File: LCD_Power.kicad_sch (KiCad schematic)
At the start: 22 parts, among them Q2 Q_PMOS_GSD, Q3 Q_PMOS_GSD, U6 SY7200AABC

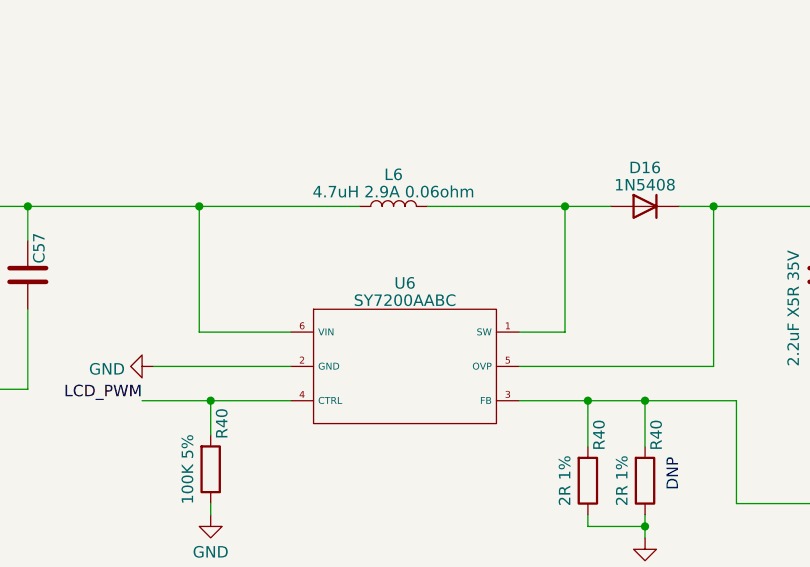
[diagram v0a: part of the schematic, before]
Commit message: updated footprints
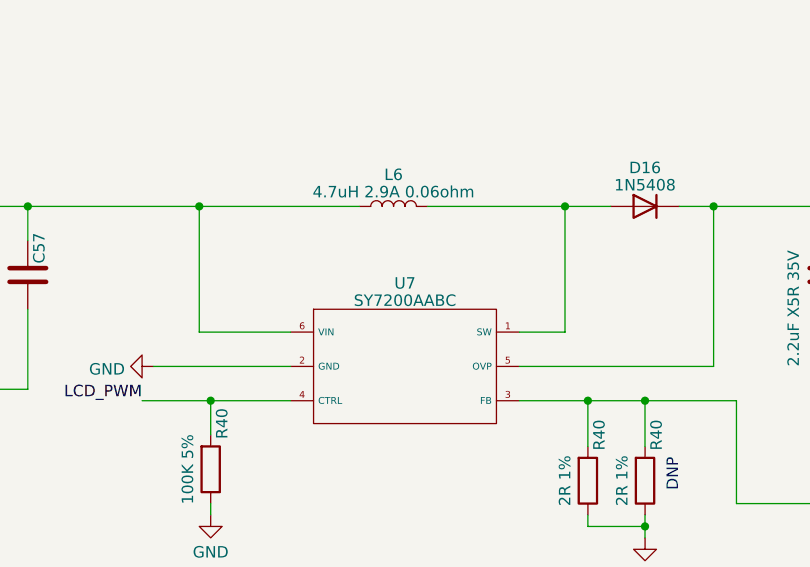
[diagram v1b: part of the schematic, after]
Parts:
- renumbered U6 to U7

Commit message: updated Reference, and PCB
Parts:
- removed D16: 1N5408, Diode_THT:D_DO-201AD_P15.24mm_Horizontal, symbol Diode:1N5408
- added D16: 1N5400, Diode_SMD:D_SOD-323, symbol Diode:1N5400
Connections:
- net VCC_LED+: now also D16.1 (K)
- net at L6.2, U7.1 (SW): now also D16.2 (A)
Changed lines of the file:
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@@
-    )
-  )
-  (symbol (lib_id "Diode:1N5408") (at 190.5 116.84 0) (mirror y) (unit 1)
-    (in_bom yes) (on_board yes) (dnp no) (fields_autoplaced)
-    (property "Reference" "D16" (at 190.5 112.5601 0)
-      (effects (font (size 1.27 1.27)))
-    )
-    (property "Value" "1N5408" (at 190.5 114.4811 0)
-      (effects (font (size 1.27 1.27)))
-    )
-    (property "Footprint" "Diode_THT:D_DO-201AD_P15.24mm_Horizontal" (at 190.5 121.285 0)
-      (effects (font (size 1.27 1.27)) hide)
-    )
-    (property "Datasheet" "http://www.vishay.com/docs/88516/1n5400.pdf" (at 190.5 116.84 0)
-      (effects (font (size 1.27 1.27)) hide)
-    )
-    (property "Sim.Device" "D" (at 190.5 116.84 0)
-      (effects (font (size 1.27 1.27)) hide)
-    )
-    (property "Sim.Pins" "1=K 2=A" (at 190.5 116.84 0)
-      (effects (font (size 1.27 1.27)) hide)
-    )
-    (pin "1")
-    (pin "2")
-    (instances
-      (project "leaf"
-        (path "/e3b58043-16a3-43c8-9fad-9c9784eebfa4/abba4c44-e9bc-404f-bbc8-3409461eb15e/42834052-256a-43ae-b5b1-2328aa6298dd"
-          (reference "D16") (unit 1)
-        )
-      )
     )
   )
@@
         )
       )
+    )
+  )
+  (symbol (lib_id "Diode:1N5400") (at 190.5 116.84 0) (mirror y) (unit 1)
+    (in_bom yes) (on_board yes) (dnp no) (fields_autoplaced)
+    (property "Reference" "D16" (at 190.5 112.5601 0)
+      (effects (font (size 1.27 1.27)))
+    )
+    (property "Value" "1N5400" (at 190.5 114.4811 0)
+      (effects (font (size 1.27 1.27)))
+    )
+    (property "Footprint" "Diode_SMD:D_SOD-323" (at 190.5 121.285 0)
+      (effects (font (size 1.27 1.27)) hide)
+    )
+    (property "Datasheet" "http://www.vishay.com/docs/88516/1n5400.pdf" (at 190.5 116.84 0)
+      (effects (font (size 1.27 1.27)) hide)
+    )
+    (property "Sim.Device" "D" (at 190.5 116.84 0)
+      (effects (font (size 1.27 1.27)) hide)
+    )
+    (property "Sim.Pins" "1=K 2=A" (at 190.5 116.84 0)
+      (effects (font (size 1.27 1.27)) hide)
+    )
+    (pin "1")
+    (pin "2")
+    (instances
+      (project "leaf"
+        (path "/e3b58043-16a3-43c8-9fad-9c9784eebfa4/abba4c44-e9bc-404f-bbc8-3409461eb15e/42834052-256a-43ae-b5b1-2328aa6298dd"
+          (reference "D16") (unit 1)
+        )
+      )

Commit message: updated Capacitors
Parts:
- C57: LCSC (none) -> C77004; Model (none) -> GRM155R61A475KEAAD; Vendor (none) -> muRata(村田)
- C57: footprint Capacitor_SMD:C_0402_1005Metric -> Capacitor_SMD:C_0201_0603Metric; LCSC (none) -> C76934; Model (none) -> GRM033R61A104KE15D; Vendor (none) -> muRata(村田)
- C57: value 4.7uF X5R 6.3V -> 4.7uF X5R 10V; LCSC (none) -> C77004; Model (none) -> GRM155R61A475KEAAD; Vendor (none) -> muRata(村田)
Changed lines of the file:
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@@
+      (effects (font (size 1.27 1.27)) hide)
+    )
+    (property "Description" "容值: 4.7uF 精度: ±10% 额定电压: 10V 材质(温度系数): X5R 材质:X5R" (at 110.49 124.46 0)
+      (effects (font (size 1.27 1.27)) hide)
+    )
+    (property "LCSC" "C77004" (at 110.49 124.46 0)
+      (effects (font (size 1.27 1.27)) hide)
+    )
+    (property "Model" "GRM155R61A475KEAAD" (at 110.49 124.46 0)
+      (effects (font (size 1.27 1.27)) hide)
+    )
+    (property "Vendor" "muRata(村田) " (at 110.49 124.46 0)
       (effects (font (size 1.27 1.27)) hide)
     )
@@
       (effects (font (size 1.27 1.27)) (justify left))
     )
-    (property "Footprint" "Capacitor_SMD:C_0402_1005Metric" (at 215.5952 55.88 0)
+    (property "Footprint" "Capacitor_SMD:C_0201_0603Metric" (at 215.5952 55.88 0)
       (effects (font (size 1.27 1.27)) hide)
     )
     (property "Datasheet" "~" (at 214.63 52.07 0)
+      (effects (font (size 1.27 1.27)) hide)
+    )
+    (property "Description" "容值: 100nF 精度: ±10% 额定电压: 10V 材质(温度系数): X5R 材质:X5R" (at 214.63 52.07 0)
+      (effects (font (size 1.27 1.27)) hide)
+    )
+    (property "LCSC" "C76934" (at 214.63 52.07 0)
+      (effects (font (size 1.27 1.27)) hide)
+    )
+    (property "Model" "GRM033R61A104KE15D" (at 214.63 52.07 0)
+      (effects (font (size 1.27 1.27)) hide)
+    )
+    (property "Vendor" "muRata(村田)" (at 214.63 52.07 0)
       (effects (font (size 1.27 1.27)) hide)
     )
@@
       (effects (font (size 1.27 1.27)) (justify left))
     )
-    (property "Value" "4.7uF X5R 6.3V" (at 138.43 62.23 90)
+    (property "Value" "4.7uF X5R 10V" (at 138.43 62.23 90)
       (effects (font (size 1.27 1.27)) (justify left))
     )
@@
     )
     (property "Datasheet" "~" (at 142.24 52.07 0)
+      (effects (font (size 1.27 1.27)) hide)
+    )
+    (property "Description" "容值: 4.7uF 精度: ±10% 额定电压: 10V 材质(温度系数): X5R 材质:X5R" (at 142.24 52.07 0)
+      (effects (font (size 1.27 1.27)) hide)
+    )
+    (property "LCSC" "C77004" (at 142.24 52.07 0)
+      (effects (font (size 1.27 1.27)) hide)
+    )
+    (property "Model" "GRM155R61A475KEAAD" (at 142.24 52.07 0)
+      (effects (font (size 1.27 1.27)) hide)
+    )
+    (property "Vendor" "muRata(村田) " (at 142.24 52.07 0)
       (effects (font (size 1.27 1.27)) hide)
     )
@@
       (effects (font (size 1.27 1.27)) (justify left))
     )
-    (property "Footprint" "Capacitor_SMD:C_0402_1005Metric" (at 122.8852 128.27 0)
+    (property "Footprint" "Capacitor_SMD:C_0201_0603Metric" (at 122.8852 128.27 0)
       (effects (font (size 1.27 1.27)) hide)
     )
     (property "Datasheet" "~" (at 121.92 124.46 0)
+      (effects (font (size 1.27 1.27)) hide)
+    )
+    (property "Description" "容值: 100nF 精度: ±10% 额定电压: 10V 材质(温度系数): X5R 材质:X5R" (at 121.92 124.46 0)
+      (effects (font (size 1.27 1.27)) hide)
+    )
+    (property "LCSC" "C76934" (at 121.92 124.46 0)
+      (effects (font (size 1.27 1.27)) hide)
+    )
+    (property "Model" "GRM033R61A104KE15D" (at 121.92 124.46 0)
+      (effects (font (size 1.27 1.27)) hide)
+    )
+    (property "Vendor" "muRata(村田)" (at 121.92 124.46 0)
       (effects (font (size 1.27 1.27)) hide)
     )
@@
       (effects (font (size 1.27 1.27)) (justify left))
     )
-    (property "Footprint" "Capacitor_SMD:C_0402_1005Metric" (at 117.8052 54.61 0)
+    (property "Footprint" "Capacitor_SMD:C_0201_0603Metric" (at 117.8052 54.61 0)
       (effects (font (size 1.27 1.27)) hide)
     )
     (property "Datasheet" "~" (at 116.84 50.8 0)
+      (effects (font (size 1.27 1.27)) hide)
+    )
+    (property "Description" "容值: 100nF 精度: ±10% 额定电压: 10V 材质(温度系数): X5R 材质:X5R" (at 116.84 50.8 0)
+      (effects (font (size 1.27 1.27)) hide)
+    )
+    (property "LCSC" "C76934" (at 116.84 50.8 0)
+      (effects (font (size 1.27 1.27)) hide)
+    )
+    (property "Model" "GRM033R61A104KE15D" (at 116.84 50.8 0)
+      (effects (font (size 1.27 1.27)) hide)
+    )
+    (property "Vendor" "muRata(村田)" (at 116.84 50.8 0)
       (effects (font (size 1.27 1.27)) hide)
     )
@@
       (effects (font (size 1.27 1.27)) (justify left))
     )
-    (property "Value" "4.7uF X5R 6.3V" (at 236.22 63.5 90)
+    (property "Value" "4.7uF X5R 10V" (at 236.22 63.5 90)
       (effects (font (size 1.27 1.27)) (justify left))
     )
@@
       (effects (font (size 1.27 1.27)) hide)
     )
+    (property "Description" "容值: 4.7uF 精度: ±10% 额定电压: 10V 材质(温度系数): X5R 材质:X5R" (at 240.03 53.34 0)
+      (effects (font (size 1.27 1.27)) hide)
+    )
+    (property "LCSC" "C77004" (at 240.03 53.34 0)
+      (effects (font (size 1.27 1.27)) hide)
+    )
+    (property "Model" "GRM155R61A475KEAAD" (at 240.03 53.34 0)
+      (effects (font (size 1.27 1.27)) hide)
+    )
+    (property "Vendor" "muRata(村田) " (at 240.03 53.34 0)
+      (effects (font (size 1.27 1.27)) hide)
+    )

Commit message: updated LCSC selection of capacitors
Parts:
- C57: LCSC (none) -> C237392; Model (none) -> GRM155R6YA225KE11D; Vendor (none) -> muRata(村田)
- C57: LCSC (none) -> C77020; Model (none) -> GRM155R71H104KE14D; Vendor (none) -> muRata(村田)
- Q2, Q3: footprint (none) -> Package_TO_SOT_SMD:SOT-23-3
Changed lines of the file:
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@@
       (effects (font (size 1.27 1.27)))
     )
-    (property "Footprint" "" (at 130.81 34.29 0)
+    (property "Footprint" "Package_TO_SOT_SMD:SOT-23-3" (at 130.81 34.29 0)
       (effects (font (size 1.27 1.27)) hide)
     )
@@
       (effects (font (size 1.27 1.27)) hide)
     )
+    (property "Description" "容值: 2.2uF 精度: ±10% 额定电压: 35V 材质(温度系数): X5R 材质:X5R" (at 210.82 124.46 0)
+      (effects (font (size 1.27 1.27)) hide)
+    )
+    (property "LCSC" "C237392" (at 210.82 124.46 0)
+      (effects (font (size 1.27 1.27)) hide)
+    )
+    (property "Model" "GRM155R6YA225KE11D" (at 210.82 124.46 0)
+      (effects (font (size 1.27 1.27)) hide)
+    )
+    (property "Vendor" "muRata(村田)" (at 210.82 124.46 0)
+      (effects (font (size 1.27 1.27)) hide)
+    )
     (pin "1")
     (pin "2")
@@
     )
     (property "Datasheet" "~" (at 248.92 53.34 0)
+      (effects (font (size 1.27 1.27)) hide)
+    )
+    (property "Description" "容值: 100nF 精度: ±10% 额定电压: 50V 材质(温度系数): X7R 材质:X7R" (at 248.92 53.34 0)
+      (effects (font (size 1.27 1.27)) hide)
+    )
+    (property "LCSC" "C77020" (at 248.92 53.34 0)
+      (effects (font (size 1.27 1.27)) hide)
+    )
+    (property "Model" "GRM155R71H104KE14D" (at 248.92 53.34 0)
+      (effects (font (size 1.27 1.27)) hide)
+    )
+    (property "Vendor" "muRata(村田)" (at 248.92 53.34 0)
       (effects (font (size 1.27 1.27)) hide)
     )
@@
       (effects (font (size 1.27 1.27)) hide)
     )
+    (property "Description" "容值: 100nF 精度: ±10% 额定电压: 50V 材质(温度系数): X7R 材质:X7R" (at 224.79 124.46 0)
+      (effects (font (size 1.27 1.27)) hide)
+    )
+    (property "LCSC" "C77020" (at 224.79 124.46 0)
+      (effects (font (size 1.27 1.27)) hide)
+    )
+    (property "Model" "GRM155R71H104KE14D" (at 224.79 124.46 0)
+      (effects (font (size 1.27 1.27)) hide)
+    )
+    (property "Vendor" "muRata(村田)" (at 224.79 124.46 0)
+      (effects (font (size 1.27 1.27)) hide)
+    )
     (pin "1")
     (pin "2")
@@
       (effects (font (size 1.27 1.27)) hide)
     )
+    (property "Description" "容值: 100nF 精度: ±10% 额定电压: 50V 材质(温度系数): X7R 材质:X7R" (at 151.13 52.07 0)
+      (effects (font (size 1.27 1.27)) hide)
+    )
+    (property "LCSC" "C77020" (at 151.13 52.07 0)
+      (effects (font (size 1.27 1.27)) hide)
+    )
+    (property "Model" "GRM155R71H104KE14D" (at 151.13 52.07 0)
+      (effects (font (size 1.27 1.27)) hide)
+    )
+    (property "Vendor" "muRata(村田)" (at 151.13 52.07 0)
+      (effects (font (size 1.27 1.27)) hide)
+    )
     (pin "1")
     (pin "2")
@@
       (effects (font (size 1.27 1.27)))
     )
-    (property "Footprint" "" (at 228.6 35.56 0)
-      (effects (font (size 1.27 1.27)) hide)
-    )
+    (property "Footprint" "Package_TO_SOT_SMD:SOT-23-3" (at 228.6 35.56 0)
+      (effects (font (size 1.27 1.27)) hide)
+    )

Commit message: updated foorprints
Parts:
- D16: value 1N5400 -> SS34 40V 3A; footprint Diode_SMD:D_SOD-323 -> Diode_SMD:D_SMA; LCSC (none) -> C8678; Model (none) -> SS34; Vendor (none) -> MDD
- L6: LCSC (none) -> C3002636; Model (none) -> CKST0603-4.7uH/M; Vendor (none) -> CENKER(岑科)
- U7: footprint (none) -> Package_TO_SOT_SMD:SOT-23-6; LCSC (none) -> C107309; Model (none) -> SY7200AABC
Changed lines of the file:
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@@
       (effects (font (size 1.27 1.27)))
     )
-    (property "Footprint" "" (at 163.83 134.62 0)
+    (property "Footprint" "Package_TO_SOT_SMD:SOT-23-6" (at 163.83 134.62 0)
       (effects (font (size 1.27 1.27)) hide)
     )
     (property "Datasheet" "" (at 163.83 134.62 0)
+      (effects (font (size 1.27 1.27)) hide)
+    )
+    (property "LCSC" "C107309" (at 163.83 134.62 0)
+      (effects (font (size 1.27 1.27)) hide)
+    )
+    (property "Model" "SY7200AABC" (at 163.83 134.62 0)
       (effects (font (size 1.27 1.27)) hide)
     )
@@
       (effects (font (size 1.27 1.27)) hide)
     )
+    (property "Description" "电感值: 4.7uH 精度: ±20% 额定电流: 5A 饱和电流(Isat): 6.5A 直流电阻(DCR): 38mΩ" (at 162.56 116.84 0)
+      (effects (font (size 1.27 1.27)) hide)
+    )
+    (property "LCSC" "C3002636" (at 162.56 116.84 0)
+      (effects (font (size 1.27 1.27)) hide)
+    )
+    (property "Model" "CKST0603-4.7uH/M" (at 162.56 116.84 0)
+      (effects (font (size 1.27 1.27)) hide)
+    )
+    (property "Vendor" "CENKER(岑科)" (at 162.56 116.84 0)
+      (effects (font (size 1.27 1.27)) hide)
+    )
     (pin "1")
     (pin "2")
@@
       (effects (font (size 1.27 1.27)))
     )
-    (property "Value" "1N5400" (at 190.5 114.4811 0)
-      (effects (font (size 1.27 1.27)))
-    )
-    (property "Footprint" "Diode_SMD:D_SOD-323" (at 190.5 121.285 0)
-      (effects (font (size 1.27 1.27)) hide)
-    )
-    (property "Datasheet" "http://www.vishay.com/docs/88516/1n5400.pdf" (at 190.5 116.84 0)
-      (effects (font (size 1.27 1.27)) hide)
-    )
-    (property "Sim.Device" "D" (at 190.5 116.84 0)
-      (effects (font (size 1.27 1.27)) hide)
-    )
-    (property "Sim.Pins" "1=K 2=A" (at 190.5 116.84 0)
-      (effects (font (size 1.27 1.27)) hide)
-    )
+    (property "Value" "SS34 40V 3A" (at 190.5 114.4811 0)
+      (effects (font (size 1.27 1.27)))
+    )
+    (property "Footprint" "Diode_SMD:D_SMA" (at 190.5 121.285 0)
+      (effects (font (size 1.27 1.27)) hide)
+    )
+    (property "Datasheet" "" (at 190.5 116.84 0)
+      (effects (font (size 1.27 1.27)) hide)
+    )
+    (property "Sim.Device" "" (at 190.5 116.84 0)
+      (effects (font (size 1.27 1.27)) hide)
+    )
+    (property "Sim.Pins" "" (at 190.5 116.84 0)
+      (effects (font (size 1.27 1.27)) hide)
+    )
+    (property "Description" "二极管配置: 独立式 直流反向耐压(Vr): 40V 平均整流电流(Io): 3A 正向压降(Vf): 0.55V@3A 反向电流(Ir):" (at 190.5 116.84 0)
+      (effects (font (size 1.27 1.27)) hide)
+    )
+    (property "LCSC" "C8678" (at 190.5 116.84 0)
+      (effects (font (size 1.27 1.27)) hide)
+    )
+    (property "Model" "SS34" (at 190.5 116.84 0)
+      (effects (font (size 1.27 1.27)) hide)
+    )
+    (property "Vendor" "MDD" (at 190.5 116.84 0)
+      (effects (font (size 1.27 1.27)) hide)
+    )

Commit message: layout SoC Power and DDR capacitors
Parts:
- C57: LCSC C76934 -> C76928; Model GRM033R61A104KE15D -> GRM033R60J104KE19D
- C57: value 100nF X5R 10V -> 100nF X5R 6.3V; LCSC C76934 -> C76928; Model GRM033R61A104KE15D -> GRM033R60J104KE19D
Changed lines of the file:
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@@
       (effects (font (size 1.27 1.27)) hide)
     )
-    (property "Description" "容值: 100nF 精度: ±10% 额定电压: 10V 材质(温度系数): X5R 材质:X5R" (at 214.63 52.07 0)
-      (effects (font (size 1.27 1.27)) hide)
-    )
-    (property "LCSC" "C76934" (at 214.63 52.07 0)
-      (effects (font (size 1.27 1.27)) hide)
-    )
-    (property "Model" "GRM033R61A104KE15D" (at 214.63 52.07 0)
+    (property "Description" "容值: 100nF 精度: ±10% 额定电压: 6.3V 材质(温度系数): X5R 材质:X5R" (at 214.63 52.07 0)
+      (effects (font (size 1.27 1.27)) hide)
+    )
+    (property "LCSC" "C76928" (at 214.63 52.07 0)
+      (effects (font (size 1.27 1.27)) hide)
+    )
+    (property "Model" "GRM033R60J104KE19D" (at 214.63 52.07 0)
       (effects (font (size 1.27 1.27)) hide)
     )
@@
       (effects (font (size 1.27 1.27)) (justify left))
     )
-    (property "Value" "100nF X5R 10V" (at 118.11 134.62 90)
+    (property "Value" "100nF X5R 6.3V" (at 118.11 134.62 90)
       (effects (font (size 1.27 1.27)) (justify left))
     )
@@
       (effects (font (size 1.27 1.27)) hide)
     )
-    (property "Description" "容值: 100nF 精度: ±10% 额定电压: 10V 材质(温度系数): X5R 材质:X5R" (at 121.92 124.46 0)
-      (effects (font (size 1.27 1.27)) hide)
-    )
-    (property "LCSC" "C76934" (at 121.92 124.46 0)
-      (effects (font (size 1.27 1.27)) hide)
-    )
-    (property "Model" "GRM033R61A104KE15D" (at 121.92 124.46 0)
+    (property "Description" "容值: 100nF 精度: ±10% 额定电压: 6.3V 材质(温度系数): X5R 材质:X5R" (at 121.92 124.46 0)
+      (effects (font (size 1.27 1.27)) hide)
+    )
+    (property "LCSC" "C76928" (at 121.92 124.46 0)
+      (effects (font (size 1.27 1.27)) hide)
+    )
+    (property "Model" "GRM033R60J104KE19D" (at 121.92 124.46 0)
       (effects (font (size 1.27 1.27)) hide)
     )
@@
       (effects (font (size 1.27 1.27)) hide)
     )
-    (property "Description" "容值: 100nF 精度: ±10% 额定电压: 10V 材质(温度系数): X5R 材质:X5R" (at 116.84 50.8 0)
-      (effects (font (size 1.27 1.27)) hide)
-    )
-    (property "LCSC" "C76934" (at 116.84 50.8 0)
-      (effects (font (size 1.27 1.27)) hide)
-    )
-    (property "Model" "GRM033R61A104KE15D" (at 116.84 50.8 0)
-      (effects (font (size 1.27 1.27)) hide)
-    )
+    (property "Description" "容值: 100nF 精度: ±10% 额定电压: 6.3V 材质(温度系数): X5R 材质:X5R" (at 116.84 50.8 0)
+      (effects (font (size 1.27 1.27)) hide)
+    )
+    (property "LCSC" "C76928" (at 116.84 50.8 0)
+      (effects (font (size 1.27 1.27)) hide)
+    )
+    (property "Model" "GRM033R60J104KE19D" (at 116.84 50.8 0)
+      (effects (font (size 1.27 1.27)) hide)
+    )

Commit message: fix some ERCs
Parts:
- renumbered C57 to C?, Q3 to Q?, Q2 to Q?, R40 to R?

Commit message: fix ERC
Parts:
- R?: now not fitted
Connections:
- net VCC_1V8: now also C?.1
- net VCC_3V3: now also C?.1
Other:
- note removed: "DNP"
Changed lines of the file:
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@@
   (junction (at 110.49 116.84) (diameter 0) (color 0 0 0 0)
   )
+  (junction (at 116.84 36.83) (diameter 0) (color 0 0 0 0)
+  )
   (junction (at 198.12 116.84) (diameter 0) (color 0 0 0 0)
   )
@@
   (junction (at 240.03 64.77) (diameter 0) (color 0 0 0 0)
   )
+  (junction (at 214.63 38.1) (diameter 0) (color 0 0 0 0)
+  )
   (junction (at 203.2 62.23) (diameter 0) (color 0 0 0 0)
   )
@@
     (stroke (width 0) (type default))
   )
-  (wire (pts (xy 203.2 38.1) (xy 220.98 38.1))
+  (wire (pts (xy 203.2 38.1) (xy 214.63 38.1))
     (stroke (width 0) (type default))
   )
@@
     (stroke (width 0) (type default))
   )
-  (wire (pts (xy 105.41 36.83) (xy 123.19 36.83))
+  (wire (pts (xy 105.41 36.83) (xy 116.84 36.83))
     (stroke (width 0) (type default))
   )
@@
     (stroke (width 0) (type default))
   )
+  (wire (pts (xy 116.84 36.83) (xy 123.19 36.83))
+    (stroke (width 0) (type default))
+  )
   (wire (pts (xy 142.24 149.86) (xy 142.24 151.13))
     (stroke (width 0) (type default))
@@
     (stroke (width 0) (type default))
   )
+  (wire (pts (xy 214.63 48.26) (xy 214.63 38.1))
+    (stroke (width 0) (type default))
+  )
   (wire (pts (xy 116.84 60.96) (xy 128.27 60.96))
     (stroke (width 0) (type default))
@@
     (stroke (width 0) (type default))
   )
+  (wire (pts (xy 116.84 36.83) (xy 116.84 46.99))
+    (stroke (width 0) (type default))
+  )
   (wire (pts (xy 134.62 138.43) (xy 142.24 138.43))
     (stroke (width 0) (type default))
@@
   )
   (wire (pts (xy 224.79 135.89) (xy 210.82 135.89))
+    (stroke (width 0) (type default))
+  )
+  (wire (pts (xy 214.63 38.1) (xy 220.98 38.1))
     (stroke (width 0) (type default))
   )
@@
     (effects (font (size 1.27 1.27)) (justify left top))
   )
-  (text "DNP" (at 194.31 148.59 90)
-    (effects (font (size 1.27 1.27) (color 194 194 0 1)) (justify left bottom))
-  )
   (label "LCD_3V3_EN" (at 176.53 62.23 180) (fields_autoplaced)
     (effects (font (size 1.27 1.27)) (justify right bottom))
@@
   )
   (symbol (lib_id "Device:R") (at 190.5 147.32 0) (mirror x) (unit 1)
-    (in_bom no) (on_board yes) (dnp no)
+    (in_bom no) (on_board yes) (dnp yes)
     (property "Reference" "R?" (at 191.77 142.24 90)
       (effects (font (size 1.27 1.27)))
